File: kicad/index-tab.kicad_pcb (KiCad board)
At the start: 2 copper layers, 254 x 140 mm, 192 parts, among them J1 USB_C_Receptacle_USB2.0, SW1 SW_Push, U1 ATmega32U4-AU, Y1 16MHz

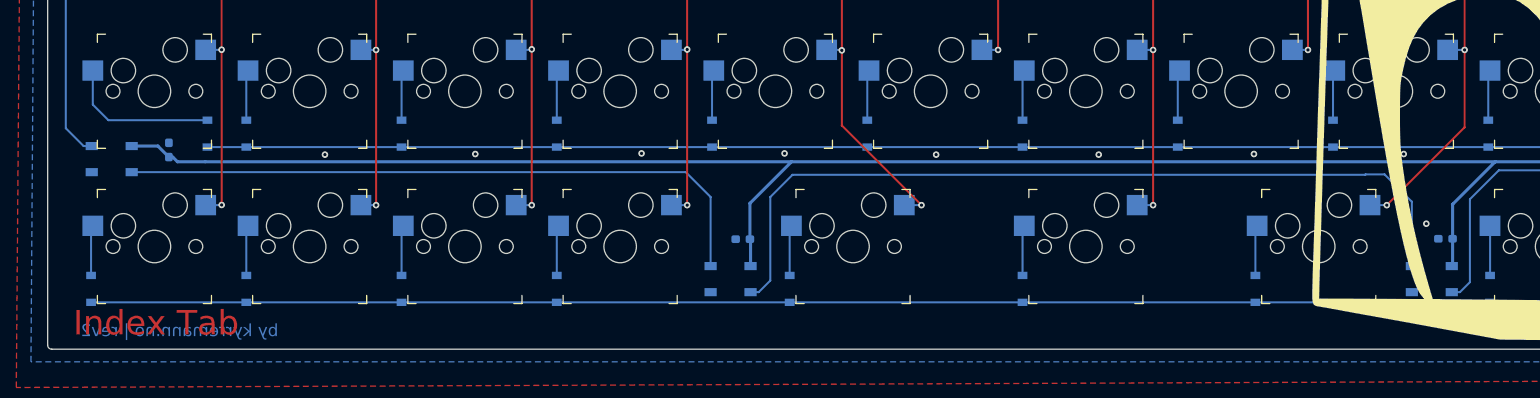
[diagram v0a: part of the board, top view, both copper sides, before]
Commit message: Added stabs and fixed text
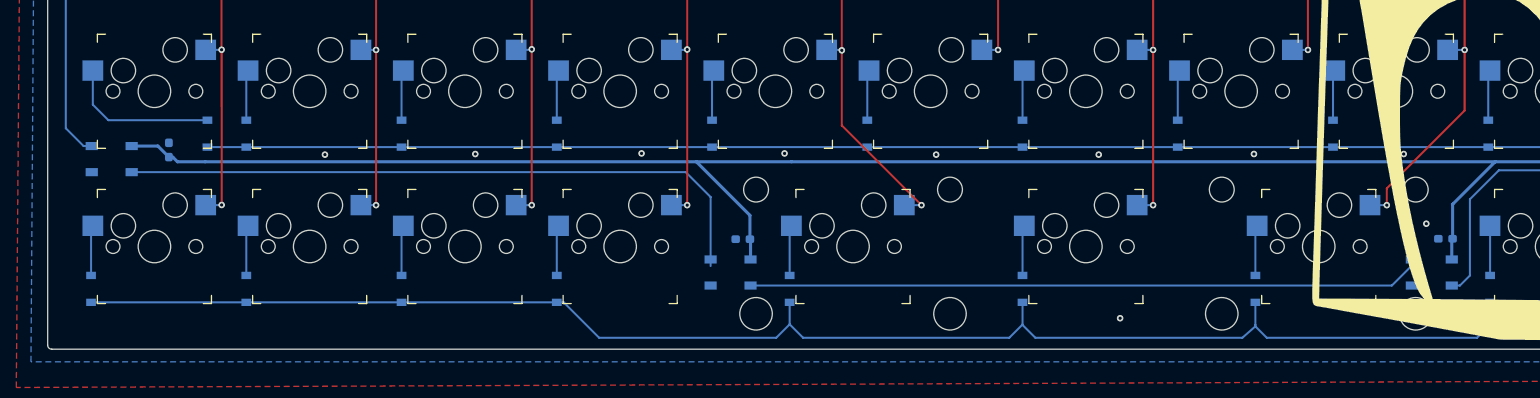
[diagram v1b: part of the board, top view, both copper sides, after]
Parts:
- added REF**: Stabilizer_MX_2u, index-tab:Stabilizer_MX_2u, F.Cu at (181.0, 152.4)
- added REF**: Stabilizer_MX_2u, index-tab:Stabilizer_MX_2u, F.Cu at (123.8, 152.4)
- moved RGB7 0.81 mm to (108.8, 155.6)
- moved RGB8 0.81 mm to (194.8, 155.6)
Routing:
- net Net-(RGB7-Pad2): track 102.4 -> 82.9 mm
- net ROW5: track 382.0 -> 399.4 mm
- net /+5v: track 940.0 -> 939.0 mm
- net Net-(RGB8-Pad2): track 86.1 -> 85.3 mm
- net GND: vias 38 -> 39
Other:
- board text added: "by kyrremann.no | rev3"
- board text removed: "by kyrremann.no | rev2"

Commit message: rotated all the rgb so they face the same direction
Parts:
- moved CR8 4.73 mm to (191.8, 151.2), turned to 0 degrees
- moved CR7 3.50 mm to (106.9, 150.8), turned to 0 degrees
- moved CR5 2.94 mm to (39.2, 104.5)
- moved CR6 1.26 mm to (41.0, 141.1)
- turned RGB5 to 0 degrees
- turned RGB6 to 0 degrees
- turned RGB7 to 0 degrees
- turned RGB8 to 0 degrees
- turned RGB9 to 0 degrees
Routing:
- net Net-(RGB6-Pad2): track 80.8 -> 103.2 mm
- net /+5v: track 939.0 -> 956.8 mm
- net Net-(RGB7-Pad2): track 82.9 -> 94.1 mm
- net Net-(RGB5-Pad2): track 41.1 -> 46.8 mm
- net Net-(RGB10-Pad4): track 43.1 -> 47.8 mm
- net Net-(RGB4-Pad2): track 41.4 -> 46.0 mm
- net GND: track 23.0 -> 27.0 mm, vias 39 -> 33
- net Net-(RGB8-Pad2): track 85.3 -> 87.4 mm

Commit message: Added screw holes to the board
Will make it easier to make better cases
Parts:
- added REF**: MountingHole_2.2mm_M2_ISO7380, MountingHole:MountingHole_2.2mm_M2_ISO7380, F.Cu at (161.7, 143.2)
- added REF**: MountingHole_2.2mm_M2_ISO7380, MountingHole:MountingHole_2.2mm_M2_ISO7380, F.Cu at (142.4, 104.9)
- added REF**: MountingHole_2.2mm_M2_ISO7380, MountingHole:MountingHole_2.2mm_M2_ISO7380, F.Cu at (161.7, 66.8)
- added REF**: MountingHole_2.2mm_M2_ISO7380, MountingHole:MountingHole_2.2mm_M2_ISO7380, F.Cu at (47.1, 66.8)
- added REF**: MountingHole_2.2mm_M2_ISO7380, MountingHole:MountingHole_2.2mm_M2_ISO7380, F.Cu at (47.1, 104.9)
- added REF**: MountingHole_2.2mm_M2_ISO7380, MountingHole:MountingHole_2.2mm_M2_ISO7380, F.Cu at (47.1, 143.2)
- added REF**: MountingHole_2.2mm_M2_ISO7380, MountingHole:MountingHole_2.2mm_M2_ISO7380, F.Cu at (257.4, 104.9)
- added REF**: MountingHole_2.2mm_M2_ISO7380, MountingHole:MountingHole_2.2mm_M2_ISO7380, F.Cu at (257.4, 143.2)
- added REF**: MountingHole_2.2mm_M2_ISO7380, MountingHole:MountingHole_2.2mm_M2_ISO7380, F.Cu at (262.4, 44.8)
- moved CR4 7.48 mm to (40.5, 67.3), turned to 90 degrees
- moved CR9 5.68 mm to (262.9, 142.9)
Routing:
- net /+5v: track 956.8 -> 970.0 mm
- net COL0: track 322.0 -> 325.8 mm
- net COL6: track 195.0 -> 198.7 mm
- net COL5: track 193.8 -> 197.2 mm
- net COL11: track 126.3 -> 128.6 mm

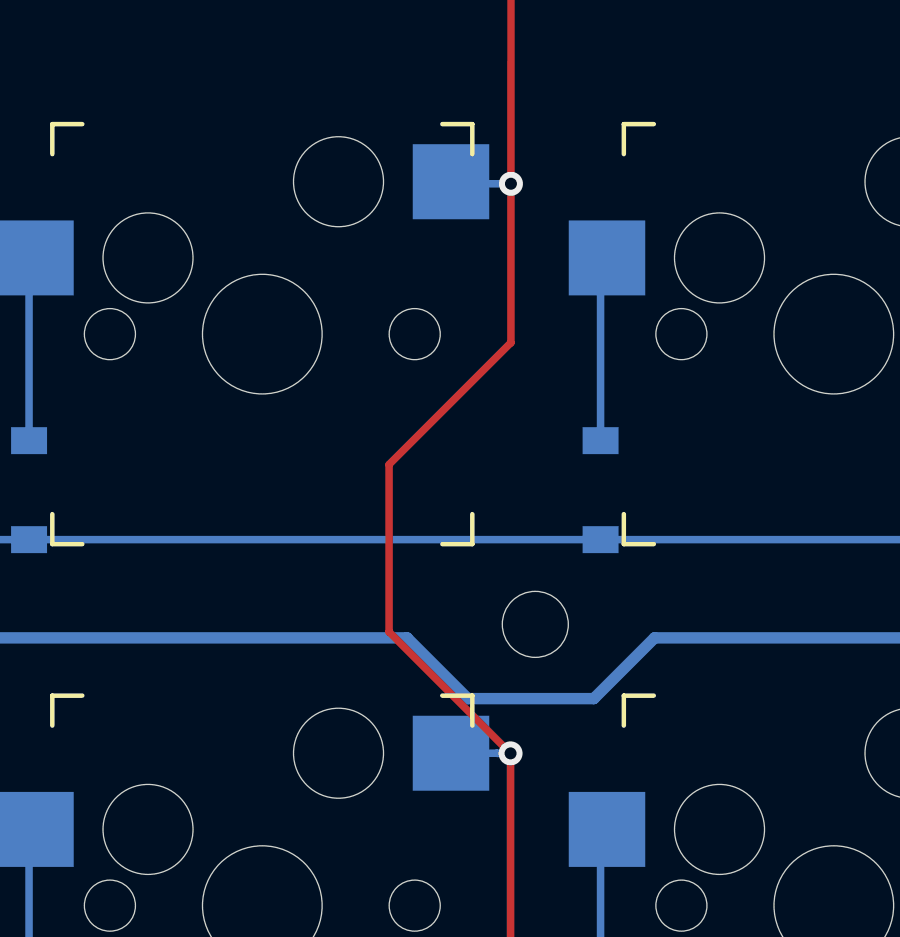
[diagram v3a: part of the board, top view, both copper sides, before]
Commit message: Fixed ugly trace
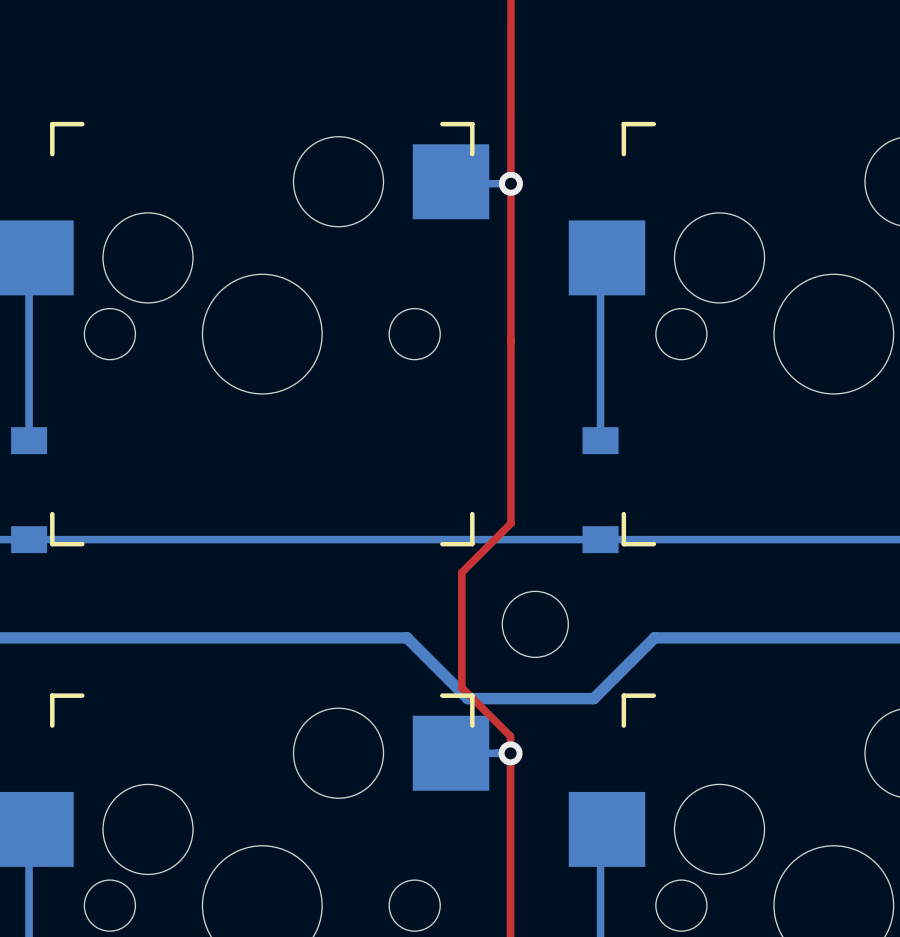
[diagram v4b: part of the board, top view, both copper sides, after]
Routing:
- net COL5: track 197.2 -> 195.3 mm
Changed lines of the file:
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@@
     (thickness 1.6)
     (drawings 16)
-    (tracks 1167)
+    (tracks 1170)
     (zones 0)
     (modules 203)
@@
   (via (at 141.625 109.225) (size 0.8) (drill 0.4) (layers F.Cu B.Cu) (net 93))
   (segment (start 141.625 128.275) (end 141.625 109.225) (width 0.25) (layer F.Cu) (net 93))
-  (segment (start 141.625 109.225) (end 137.575 105.175) (width 0.25) (layer F.Cu) (net 93))
-  (segment (start 137.575 105.175) (end 137.575 99.6) (width 0.25) (layer F.Cu) (net 93))
-  (segment (start 141.637479 95.537521) (end 141.637479 90.237479) (width 0.25) (layer F.Cu) (net 93))
-  (segment (start 137.575 99.6) (end 141.637479 95.537521) (width 0.25) (layer F.Cu) (net 93))
+  (segment (start 141.625 108.659315) (end 140 107.034315) (width 0.25) (layer F.Cu) (net 93))
+  (segment (start 141.625 109.225) (end 141.625 108.659315) (width 0.25) (layer F.Cu) (net 93))
+  (segment (start 140 107.034315) (end 140 103.2) (width 0.25) (layer F.Cu) (net 93))
+  (segment (start 141.637479 101.562521) (end 141.637479 95.437521) (width 0.25) (layer F.Cu) (net 93))
+  (segment (start 140 103.2) (end 141.637479 101.562521) (width 0.25) (layer F.Cu) (net 93))
+  (segment (start 141.637479 95.537521) (end 141.637479 95.437521) (width 0.25) (layer F.Cu) (net 93))
+  (segment (start 141.637479 95.437521) (end 141.637479 90.237479) (width 0.25) (layer F.Cu) (net 93))
   (segment (start 160.215 52.07) (end 160.235 52.05) (width 0.25) (layer B.Cu) (net 94))
   (segment (start 158.69 52.07) (end 160.215 52.07) (width 0.25) (layer B.Cu) (net 94))

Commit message: Adding crazy many options for bottom row
this is going to be rev4
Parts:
- removed G***: LOGO, index-tab:monster
- removed the REF** at (161.7, 143.2)
- removed the REF** at (181.0, 152.4)
- removed the REF** at (123.8, 152.4)
- removed the REF** at (142.4, 104.9)
- removed the REF** at (161.7, 66.8)
- removed the REF** at (47.1, 66.8)
- removed the REF** at (47.1, 104.9)
- removed the REF** at (47.1, 143.2)
- removed the REF** at (257.4, 104.9)
- removed the REF** at (257.4, 143.2)
- removed the REF** at (262.4, 44.8)
- added D77: 1N4148W, Diode_SMD:D_SOD-123, B.Cu at (127.0, 161.9)
- added D78: 1N4148W, Diode_SMD:D_SOD-123, B.Cu at (165.1, 161.9)
- added MX77: MX-NoLED, index-tab:Kailh_socket_MX, F.Cu at (133.3, 152.4)
- added MX78: MX-NoLED, index-tab:Kailh_socket_MX, F.Cu at (171.4, 152.4)
- added MX79: MX-NoLED, index-tab:Kailh_socket_MX, F.Cu at (104.8, 152.4)
- added MX80: MX-NoLED, index-tab:Kailh_socket_MX, F.Cu at (123.8, 152.4)
- added MX81: MX-NoLED, index-tab:Kailh_socket_MX, F.Cu at (142.9, 152.4)
- added MX82: MX-NoLED, index-tab:Kailh_socket_MX, F.Cu at (161.9, 152.4)
- added MX83: MX-NoLED, index-tab:Kailh_socket_MX, F.Cu at (181.0, 152.4)
- added MX84: MX-NoLED, index-tab:Kailh_socket_MX, F.Cu at (200.0, 152.4)
- added REF**: 7U, index-tab:MXOnly-7U-Hotswap, F.Cu at (152.4, 152.4)
- moved RGB8 23.9 mm to (212.7, 139.7)
- moved CR8 20.7 mm to (206.4, 136.5)
- moved CR7 19.0 mm to (92.8, 138.1)
- moved RGB7 18.9 mm to (98.5, 139.7)
- moved D52 11.8 mm to (184.2, 161.9)
- moved MX30 9.53 mm to (114.3, 152.4)
- moved MX52 9.53 mm to (190.5, 152.4)
- moved D30 9.18 mm to (108.0, 161.9)
- moved D64 6.77 mm to (227.0, 160.3)
- moved D41 4.55 mm to (146.1, 161.9)
- moved D58 4.49 mm to (203.2, 161.9)
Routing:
- net ROW5: track 399.4 -> 229.6 mm
- net Net-(RGB7-Pad2): track 94.1 -> 0.00 mm
- net Net-(RGB8-Pad2): track 87.4 -> 0.00 mm
- net Net-(RGB6-Pad2): track 103.2 -> 20.3 mm
- net /+5v: track 970.0 -> 928.3 mm
- net COL5: track 195.3 -> 216.5 mm, vias 6 -> 7
- net COL7: track 154.3 -> 175.4 mm, vias 6 -> 7
- net Net-(D58-Pad2): track 6.09 -> 0.01 mm
- net Net-(D30-Pad2): track 6.18 -> 0.30 mm
- net Net-(D64-Pad2): track 6.18 -> 0.30 mm
- net Net-(D52-Pad2): track 6.18 -> 0.30 mm
- net COL4: track 238.0 -> 233.7 mm
- net COL8: track 162.0 -> 158.2 mm
- net COL6: track 198.7 -> 196.4 mm
- net GND: track 27.0 -> 25.5 mm, vias 33 -> 26
